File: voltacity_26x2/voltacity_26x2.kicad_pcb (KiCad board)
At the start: 2 copper layers, 323.1 x 125.1 mm, 190 parts, among them J1 2-Pin JST, J4 78127-1128, SW1 Switch, SW2 RotaryEncoder, SW3 RotaryEncoder, SW4 RotaryEncoder

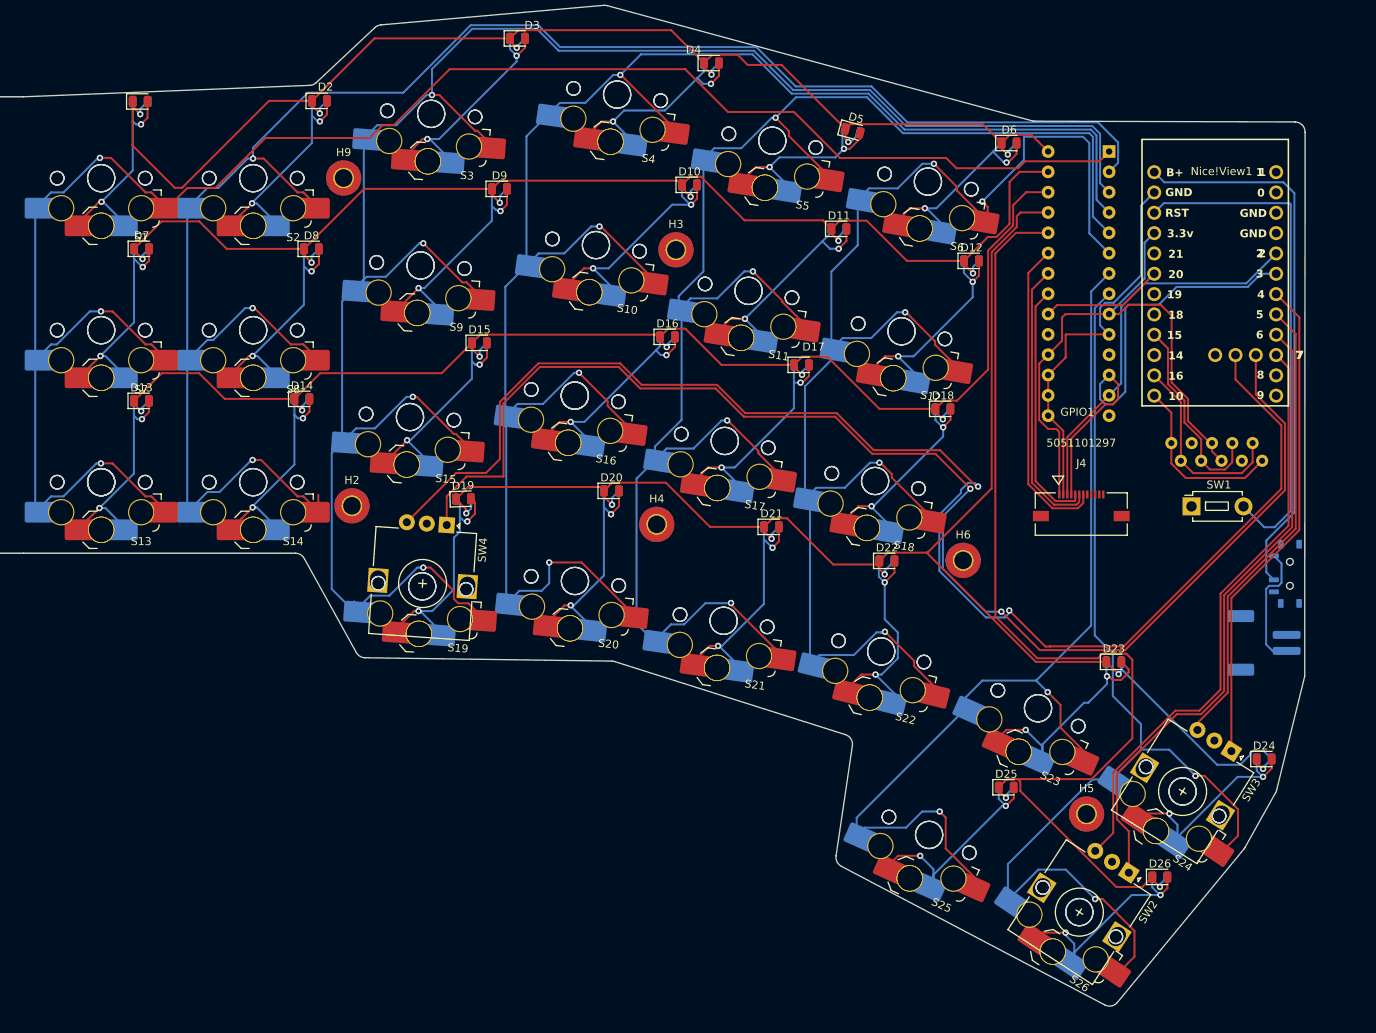
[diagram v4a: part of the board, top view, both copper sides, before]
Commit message: Removed unneeded files
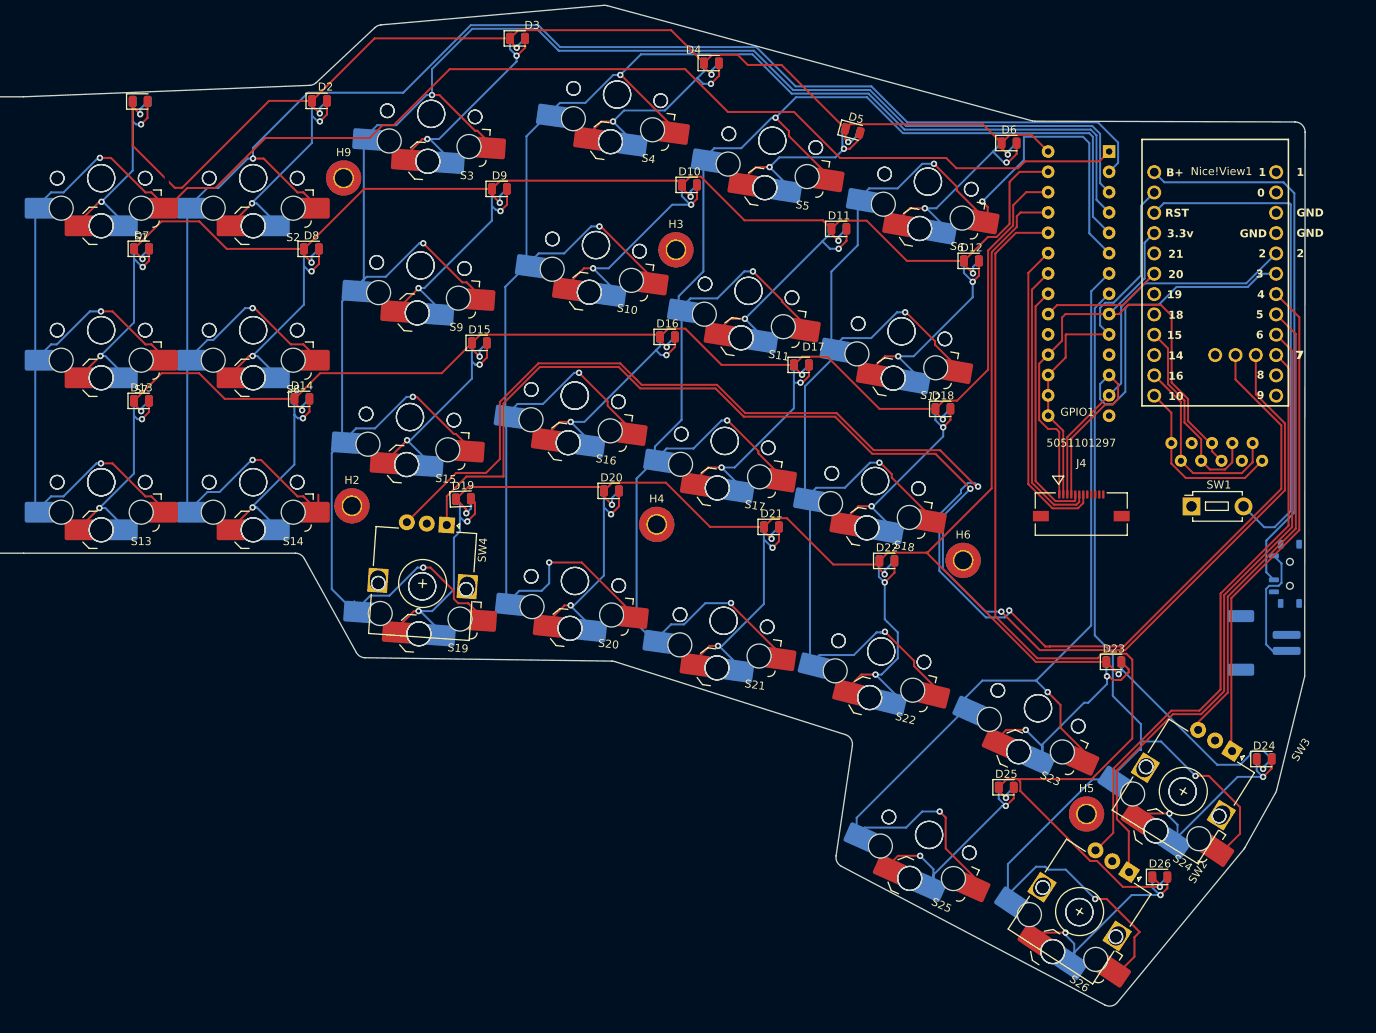
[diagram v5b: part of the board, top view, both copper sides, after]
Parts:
- moved SW3 7.98 mm to (367.4, 193.3)
- moved SW2 7.98 mm to (354.5, 208.5)
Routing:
- net Thu_Col_2: track 135.6 -> 137.8 mm
